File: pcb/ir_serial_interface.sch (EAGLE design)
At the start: 26 parts, among them IC1 PIC18F2550_28W, Q1 BSS123, T1 SFH303

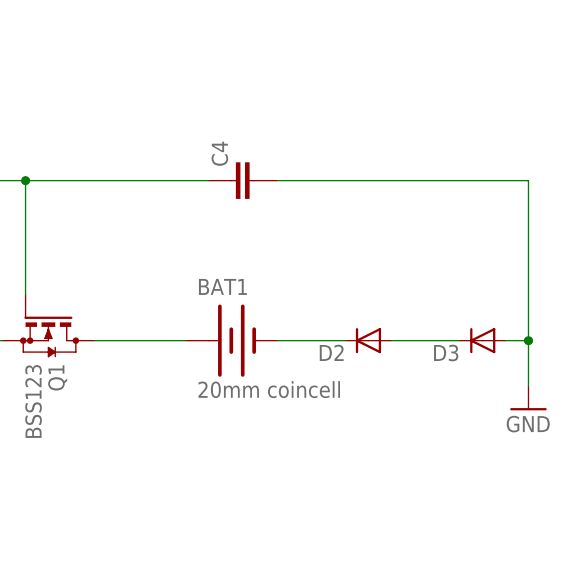
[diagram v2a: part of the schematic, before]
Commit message: sleep longer after fsk tx
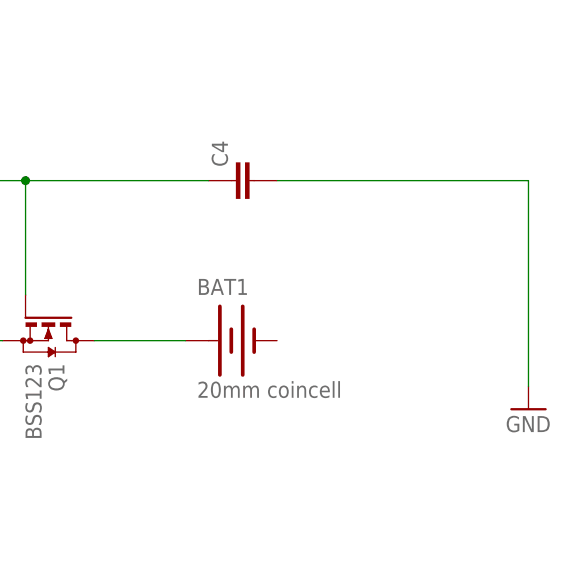
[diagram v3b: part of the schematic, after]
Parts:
- removed D2, D3: (no value), SparkFun-DiscreteSemi:DIODESOT23
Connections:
- removed net N$12: BAT1.-, D2.C
- removed net N$13: D2.A, D3.C
- net GND: no longer D3.A
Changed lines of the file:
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@@
 <part name="R8" library="resistor" deviceset="R-EU_" device="M0805" value="190"/>
 <part name="BAT1" library="SparkFun-Electromechanical" deviceset="BATTERY" device="20PTH" value="20mm coincell"/>
-<part name="D2" library="SparkFun-DiscreteSemi" deviceset="DIODE" device="SOT23"/>
-<part name="D3" library="SparkFun-DiscreteSemi" deviceset="DIODE" device="SOT23"/>
 <part name="P+5" library="supply1" deviceset="+5V" device=""/>
 <part name="GND10" library="supply1" deviceset="GND" device=""/>
@@
 <instance part="R8" gate="G$1" x="134.62" y="60.96" rot="R90"/>
 <instance part="BAT1" gate="G$1" x="289.56" y="12.7"/>
-<instance part="D2" gate="G$1" x="304.8" y="12.7" rot="R180"/>
-<instance part="D3" gate="G$1" x="317.5" y="12.7" rot="R180"/>
 <instance part="P+5" gate="1" x="251.46" y="22.86"/>
 <instance part="GND10" gate="1" x="322.58" y="5.08"/>
@@
 </segment>
 <segment>
-<pinref part="D3" gate="G$1" pin="A"/>
 <pinref part="GND10" gate="1" pin="GND"/>
-<wire x1="320.04" y1="12.7" x2="322.58" y2="12.7" width="0.1524" layer="91"/>
-<wire x1="322.58" y1="12.7" x2="322.58" y2="7.62" width="0.1524" layer="91"/>
 <pinref part="C4" gate="G$1" pin="2"/>
 <wire x1="294.64" y1="30.48" x2="322.58" y2="30.48" width="0.1524" layer="91"/>
-<wire x1="322.58" y1="30.48" x2="322.58" y2="12.7" width="0.1524" layer="91"/>
-<junction x="322.58" y="12.7"/>
+<wire x1="322.58" y1="30.48" x2="322.58" y2="7.62" width="0.1524" layer="91"/>
 </segment>
 <segment>
@@
 </segment>
 </net>
-<net name="N$12" class="0">
-<segment>
-<pinref part="BAT1" gate="G$1" pin="-"/>
-<pinref part="D2" gate="G$1" pin="C"/>
-<wire x1="294.64" y1="12.7" x2="302.26" y2="12.7" width="0.1524" layer="91"/>
-</segment>
-</net>
-<net name="N$13" class="0">
-<segment>
-<pinref part="D2" gate="G$1" pin="A"/>
-<pinref part="D3" gate="G$1" pin="C"/>
-<wire x1="307.34" y1="12.7" x2="314.96" y2="12.7" width="0.1524" layer="91"/>
-</segment>
-</net>

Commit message: multical iii docs + pcb
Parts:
- R4: value 200k -> 100k; device resistor:R-TRIMM3214W -> resistor:R-EU_M0805
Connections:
- net GND: now also R4.1; no longer R4.E
- net N$6: now also R4.2; no longer R4.S
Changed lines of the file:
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@@
 <part name="P+5" library="supply1" deviceset="+5V" device=""/>
 <part name="GND10" library="supply1" deviceset="GND" device=""/>
-<part name="R4" library="resistor" deviceset="R-TRIMM" device="3214W" value="200k"/>
 <part name="R9" library="resistor" deviceset="R-EU_" device="M0805" value="190"/>
 <part name="D4" library="led" deviceset="LED" device="3MM" value="IR"/>
@@
 <part name="Q1" library="transistor-small-signal" deviceset="BSS123" device=""/>
 <part name="C4" library="rcl" deviceset="C-EU" device="C0805"/>
+<part name="R4" library="resistor" deviceset="R-EU_" device="M0805" value="100k"/>
 </parts>
 <sheets>
@@
 <instance part="P+4" gate="1" x="203.2" y="96.52"/>
 <instance part="GND4" gate="1" x="226.06" y="53.34"/>
-<instance part="GND5" gate="1" x="198.12" y="53.34"/>
+<instance part="GND5" gate="1" x="203.2" y="53.34"/>
 <instance part="GND6" gate="1" x="185.42" y="53.34"/>
 <instance part="C3" gate="G$1" x="205.74" y="129.54" rot="R90"/>
@@
 <instance part="P+5" gate="1" x="251.46" y="22.86"/>
 <instance part="GND10" gate="1" x="322.58" y="5.08"/>
-<instance part="R4" gate="G$1" x="198.12" y="63.5"/>
 <instance part="R9" gate="G$1" x="137.16" y="48.26" rot="R90"/>
 <instance part="D4" gate="G$1" x="142.24" y="53.34" rot="R90"/>
@@
 <instance part="Q1" gate="G$1" x="269.24" y="12.7" rot="R270"/>
 <instance part="C4" gate="G$1" x="289.56" y="30.48" rot="R90"/>
+<instance part="R4" gate="G$1" x="203.2" y="66.04" rot="R90"/>
 </instances>
 <busses>
@@
 </segment>
 <segment>
-<pinref part="R4" gate="G$1" pin="E"/>
-<pinref part="GND5" gate="1" pin="GND"/>
-<wire x1="198.12" y1="58.42" x2="198.12" y2="55.88" width="0.1524" layer="91"/>
-</segment>
-<segment>
 <pinref part="D4" gate="G$1" pin="C"/>
 <pinref part="GND11" gate="1" pin="GND"/>
 <wire x1="147.32" y1="53.34" x2="149.86" y2="53.34" width="0.1524" layer="91"/>
 <wire x1="149.86" y1="53.34" x2="149.86" y2="50.8" width="0.1524" layer="91"/>
+</segment>
+<segment>
+<pinref part="R4" gate="G$1" pin="1"/>
+<pinref part="GND5" gate="1" pin="GND"/>
+<wire x1="203.2" y1="60.96" x2="203.2" y2="55.88" width="0.1524" layer="91"/>
 </segment>
 </net>
@@
 <pinref part="IC1" gate="G$1" pin="RA0/AN0"/>
 <wire x1="50.8" y1="35.56" x2="55.88" y2="35.56" width="0.1524" layer="91"/>
-<pinref part="R4" gate="G$1" pin="S"/>
-<wire x1="203.2" y1="63.5" x2="203.2" y2="73.66" width="0.1524" layer="91"/>
-</segment>
-</net>
+<pinref part="R4" gate="G$1" pin="2"/>
+<wire x1="203.2" y1="71.12" x2="203.2" y2="73.66" width="0.1524" layer="91"/>
+</segment>
+</net>

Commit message: PCB: board layout done
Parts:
- removed GND, LEFT, MIC, RIGHT: LSP10, solpad:LSP10
- removed Q1: BSS123, transistor-small-signal:BSS123
- added D2: (no value), semicon-smd-ipc:D-A1-C3
- added IC2: LP2992, texas:TPS77001
- added Q2: BC847SMD, transistor-npn:BC847SMD
- added R10: 2k, resistor:R-EU_M0805
- added R11, R12, R13: 100k, resistor:R-EU_M0805
- added U$2: AUDIO-JACK3, SparkFun-Connectors:AUDIO-JACK3
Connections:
- new net N$12: D2.A, U$2.RING1
- new net N$13: IC2.!EN, Q2.E, R11.1
- new net N$18: C4.1, D2.C, R10.2
- new net V+: BAT1.+, IC2.IN, Q2.C, R13.2
- net +5V: now also IC2.OUT; no longer Q1.S
- net GND: now also BAT1.-, IC2.GND, R11.2, R12.1, U$2.RING2; no longer GND.MP
- net N$16: now also IC1.RA5/AN4/!SS!/HLVDIN/C2OUT, R12.2, R13.1; no longer BAT1.+, Q1.D
- net N$17: now also Q2.B, R10.1; no longer C4.1, Q1.G, RIGHT.MP
- net N$5: now also U$2.TIP; no longer LEFT.MP
- net N$7: now also U$2.EARTH; no longer MIC.MP
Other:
- moved on the sheet: BAT1, C1, C2, C3, C4, R3, R4, R5, R6, R7

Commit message: silk screen cleanup
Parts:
- removed D4: IR, led:LED3MM
- added D3: (no value), semicon-smd-ipc:D-A1-C3
- D1: value RED -> IR; device SparkFun-LED:LED-REDLILYPAD -> led:LED3MM
- D2: value (none) -> RED; device semicon-smd-ipc:D-A1-C3 -> SparkFun-LED:LED-REDLILYPAD
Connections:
- net GND: now also D2.C; no longer D4.C
- net N$10: now also D2.A; no longer D1.A
- net N$12: now also D3.A; no longer D2.A
- net N$14: now also D1.A; no longer D4.A
- net N$18: now also D3.C; no longer D2.C
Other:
- moved on the sheet: D1
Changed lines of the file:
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@@
 <part name="GND7" library="supply1" deviceset="GND" device=""/>
 <part name="GND8" library="supply1" deviceset="GND" device=""/>
-<part name="D1" library="SparkFun-LED" deviceset="LED-RED" device="LILYPAD" value="RED"/>
+<part name="D2" library="SparkFun-LED" deviceset="LED-RED" device="LILYPAD" value="RED"/>
 <part name="GND9" library="supply1" deviceset="GND" device=""/>
 <part name="R8" library="resistor" deviceset="R-EU_" device="M0805" value="190"/>
@@
 <part name="GND10" library="supply1" deviceset="GND" device=""/>
 <part name="R9" library="resistor" deviceset="R-EU_" device="M0805" value="190"/>
-<part name="D4" library="led" deviceset="LED" device="3MM" value="IR"/>
+<part name="D1" library="led" deviceset="LED" device="3MM" value="IR"/>
 <part name="GND11" library="supply1" deviceset="GND" device=""/>
 <part name="C4" library="rcl" deviceset="C-EU" device="C0805"/>
@@
 <part name="GND12" library="supply1" deviceset="GND" device=""/>
 <part name="Q2" library="transistor-npn" deviceset="BC847*" device="SMD"/>
-<part name="D2" library="semicon-smd-ipc" deviceset="D-" device="A1-C3"/>
+<part name="D3" library="semicon-smd-ipc" deviceset="D-" device="A1-C3"/>
 <part name="GND4" library="supply1" deviceset="GND" device=""/>
 <part name="R10" library="resistor" deviceset="R-EU_" device="M0805" value="2k"/>
@@
 <instance part="GND7" gate="1" x="86.36" y="58.42"/>
 <instance part="GND8" gate="1" x="68.58" y="58.42"/>
-<instance part="D1" gate="G$1" x="142.24" y="66.04" rot="R90"/>
+<instance part="D2" gate="G$1" x="142.24" y="66.04" rot="R90"/>
 <instance part="GND9" gate="1" x="149.86" y="60.96"/>
 <instance part="R8" gate="G$1" x="134.62" y="60.96" rot="R90"/>
@@
 <instance part="GND10" gate="1" x="172.72" y="63.5"/>
 <instance part="R9" gate="G$1" x="137.16" y="48.26" rot="R90"/>
-<instance part="D4" gate="G$1" x="142.24" y="53.34" rot="R90"/>
+<instance part="D1" gate="G$1" x="142.24" y="53.34" rot="R90"/>
 <instance part="GND11" gate="1" x="149.86" y="48.26"/>
 <instance part="C4" gate="G$1" x="172.72" y="78.74"/>
@@
 <instance part="GND12" gate="1" x="106.68" y="116.84"/>
 <instance part="Q2" gate="G$1" x="203.2" y="91.44"/>
-<instance part="D2" gate="G$1" x="162.56" y="91.44"/>
+<instance part="D3" gate="G$1" x="162.56" y="91.44"/>
 <instance part="GND4" gate="1" x="205.74" y="63.5"/>
 <instance part="R10" gate="G$1" x="185.42" y="91.44" rot="R180"/>
@@
 </segment>
 <segment>
-<pinref part="D1" gate="G$1" pin="C"/>
+<pinref part="D2" gate="G$1" pin="C"/>
 <pinref part="GND9" gate="1" pin="GND"/>
 <wire x1="147.32" y1="66.04" x2="149.86" y2="66.04" width="0.1524" layer="91"/>
@@
 </segment>
 <segment>
-<pinref part="D4" gate="G$1" pin="C"/>
+<pinref part="D1" gate="G$1" pin="C"/>
 <pinref part="GND11" gate="1" pin="GND"/>
 <wire x1="147.32" y1="53.34" x2="149.86" y2="53.34" width="0.1524" layer="91"/>
@@
 <net name="N$10" class="0">
 <segment>
-<pinref part="D1" gate="G$1" pin="A"/>
+<pinref part="D2" gate="G$1" pin="A"/>
 <pinref part="R8" gate="G$1" pin="2"/>
 <wire x1="139.7" y1="66.04" x2="134.62" y2="66.04" width="0.1524" layer="91"/>
@@
 <net name="N$14" class="0">
 <segment>
-<pinref part="D4" gate="G$1" pin="A"/>
+<pinref part="D1" gate="G$1" pin="A"/>
 <pinref part="R9" gate="G$1" pin="2"/>
 <wire x1="139.7" y1="53.34" x2="137.16" y2="53.34" width="0.1524" layer="91"/>
@@
 <net name="N$12" class="0">
 <segment>
-<pinref part="D2" gate="G$1" pin="A"/>
+<pinref part="D3" gate="G$1" pin="A"/>
 <wire x1="160.02" y1="91.44" x2="116.84" y2="91.44" width="0.1524" layer="91"/>
 <wire x1="116.84" y1="91.44" x2="116.84" y2="111.76" width="0.1524" layer="91"/>
@@
 <net name="N$18" class="0">
 <segment>
-<pinref part="D2" gate="G$1" pin="C"/>
+<pinref part="D3" gate="G$1" pin="C"/>
 <pinref part="R10" gate="G$1" pin="2"/>
 <wire x1="165.1" y1="91.44" x2="172.72" y2="91.44" width="0.1524" layer="91"/>

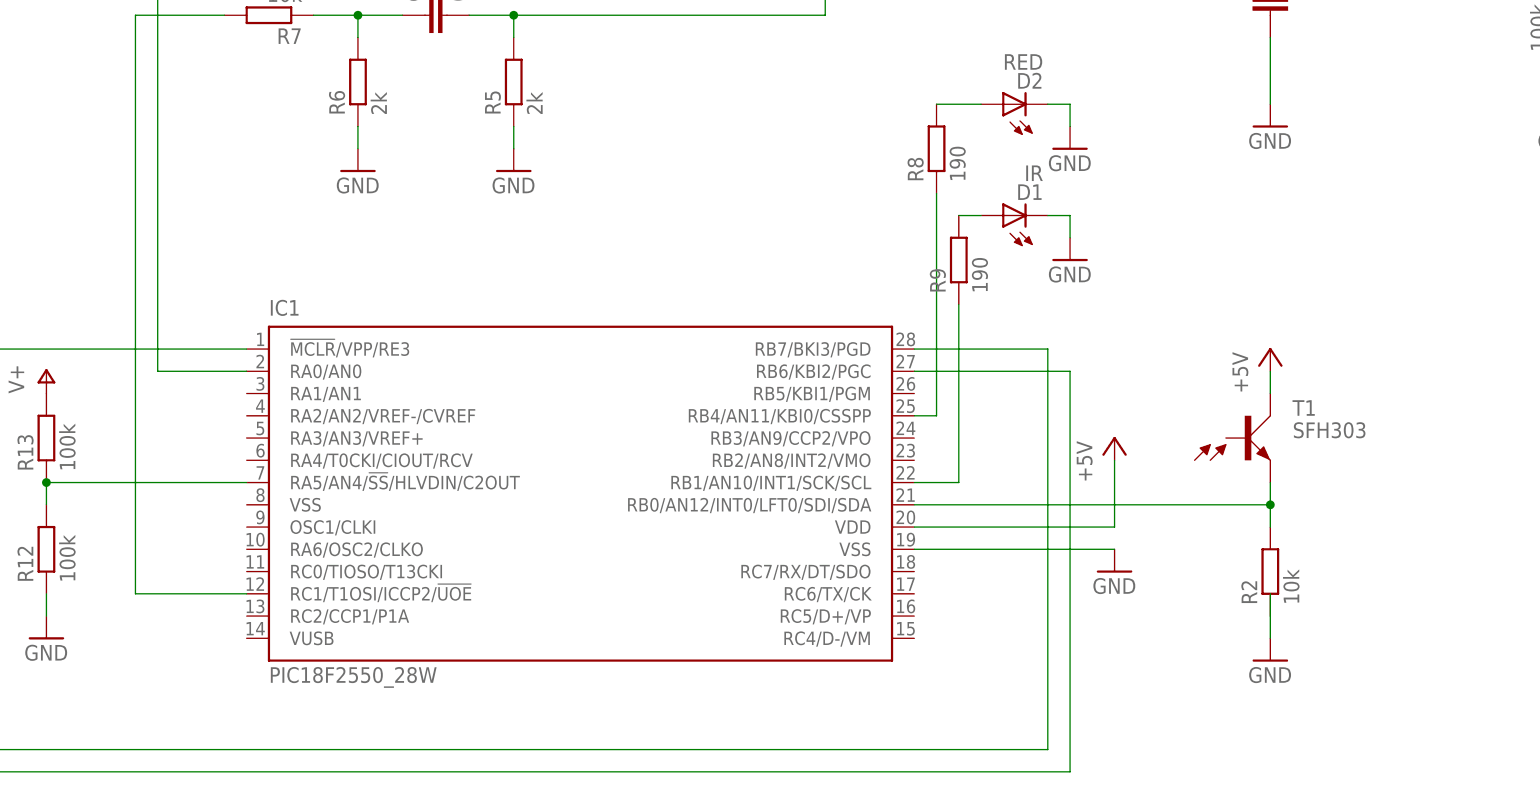
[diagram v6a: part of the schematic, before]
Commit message: cut round - wider outline path
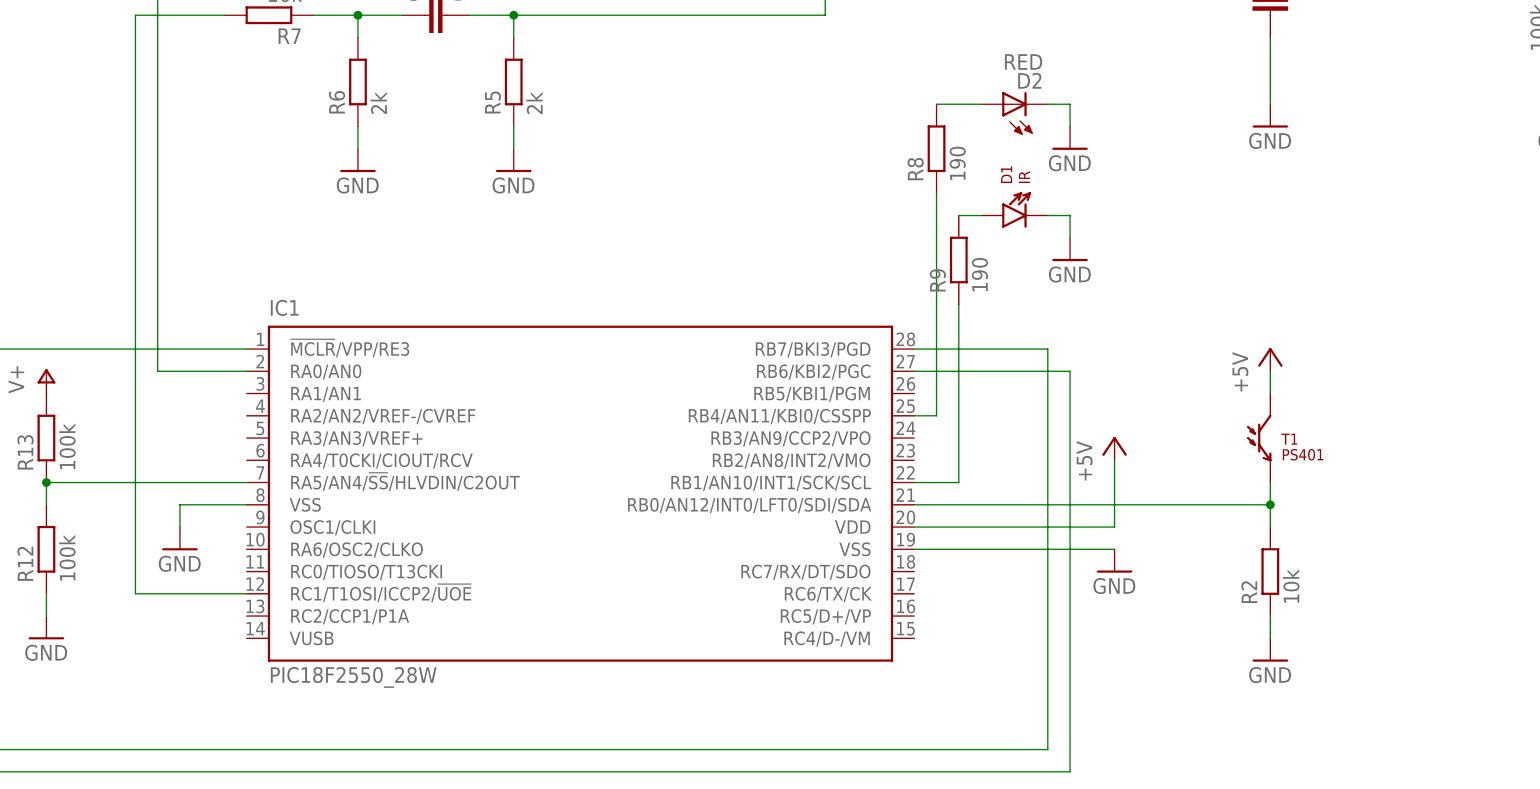
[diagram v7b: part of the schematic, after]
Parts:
- D1: device led:LED3MM -> SparkFun-LED:LTE-302
- T1: value SFH303 -> PS401; device opto-trans-siemens:SFH303 -> SparkFun-Sensors:LTR-301
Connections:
- net GND: now also IC1.VSS
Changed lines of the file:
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@@
 <layer number="54" name="bGND_GNDA" color="1" fill="9" visible="no" active="no"/>
 <layer number="56" name="wert" color="7" fill="1" visible="no" active="no"/>
+<layer number="57" name="tCAD" color="7" fill="1" visible="no" active="no"/>
 <layer number="91" name="Nets" color="2" fill="1" visible="yes" active="yes"/>
 <layer number="92" name="Busses" color="1" fill="1" visible="yes" active="yes"/>
@@
 <layer number="97" name="Info" color="7" fill="1" visible="yes" active="yes"/>
 <layer number="98" name="Guide" color="6" fill="1" visible="yes" active="yes"/>
+<layer number="99" name="SpiceOrder" color="7" fill="1" visible="yes" active="yes"/>
 <layer number="100" name="Muster" color="7" fill="1" visible="no" active="no"/>
 <layer number="101" name="Patch_Top" color="12" fill="4" visible="yes" active="yes"/>
@@
 <layer number="108" name="tplace-old" color="10" fill="1" visible="yes" active="yes"/>
 <layer number="109" name="ref-old" color="11" fill="1" visible="yes" active="yes"/>
+<layer number="110" name="fp0" color="7" fill="1" visible="yes" active="yes"/>
+<layer number="111" name="LPC17xx" color="7" fill="1" visible="yes" active="yes"/>
+<layer number="112" name="tSilk" color="7" fill="1" visible="yes" active="yes"/>
 <layer number="116" name="Patch_BOT" color="9" fill="4" visible="yes" active="yes"/>
 <layer number="121" name="_tsilk" color="7" fill="1" visible="yes" active="yes"/>
 <layer number="122" name="_bsilk" color="7" fill="1" visible="yes" active="yes"/>
+<layer number="123" name="tTestmark" color="7" fill="1" visible="yes" active="yes"/>
+<layer number="124" name="bTestmark" color="7" fill="1" visible="yes" active="yes"/>
 <layer number="125" name="_tNames" color="7" fill="1" visible="yes" active="yes"/>
+<layer number="126" name="_bNames" color="7" fill="1" visible="yes" active="yes"/>
+<layer number="127" name="_tValues" color="7" fill="1" visible="yes" active="yes"/>
+<layer number="128" name="_bValues" color="7" fill="1" visible="yes" active="yes"/>
+<layer number="131" name="tAdjust" color="7" fill="1" visible="yes" active="yes"/>
+<layer number="132" name="bAdjust" color="7" fill="1" visible="yes" active="yes"/>
 <layer number="144" name="Drill_legend" color="7" fill="1" visible="yes" active="yes"/>
+<layer number="150" name="Notes" color="7" fill="1" visible="yes" active="yes"/>
 <layer number="151" name="HeatSink" color="7" fill="1" visible="yes" active="yes"/>
+<layer number="152" name="_bDocu" color="7" fill="1" visible="yes" active="yes"/>
+<layer number="153" name="FabDoc1" color="7" fill="1" visible="yes" active="yes"/>
+<layer number="154" name="FabDoc2" color="7" fill="1" visible="yes" active="yes"/>
+<layer number="155" name="FabDoc3" color="7" fill="1" visible="yes" active="yes"/>
 <layer number="199" name="Contour" color="7" fill="1" visible="yes" active="yes"/>
 <layer number="200" name="200bmp" color="1" fill="10" visible="yes" active="yes"/>
@@
 <layer number="223" name="223bmp" color="24" fill="1" visible="no" active="no"/>
 <layer number="224" name="224bmp" color="25" fill="1" visible="no" active="no"/>
+<layer number="248" name="Housing" color="7" fill="1" visible="yes" active="yes"/>
+<layer number="249" name="Edge" color="7" fill="1" visible="yes" active="yes"/>
 <layer number="250" name="Descript" color="3" fill="1" visible="no" active="no"/>
 <layer number="251" name="SMDround" color="12" fill="11" visible="no" active="no"/>
@@
 </classes>
 <parts>
-<part name="T1" library="opto-trans-siemens" deviceset="SFH303" device=""/>
+<part name="T1" library="SparkFun-Sensors" deviceset="LTR-301" device="" value="PS401"/>
 <part name="P+1" library="supply1" deviceset="+5V" device=""/>
 <part name="GND1" library="supply1" deviceset="GND" device=""/>
@@
 <part name="GND10" library="supply1" deviceset="GND" device=""/>
 <part name="R9" library="resistor" deviceset="R-EU_" device="M0805" value="190"/>
-<part name="D1" library="led" deviceset="LED" device="3MM" value="IR"/>
+<part name="D1" library="SparkFun-LED" deviceset="LTE-302" device="" value="IR"/>
 <part name="GND11" library="supply1" deviceset="GND" device=""/>
 <part name="C4" library="rcl" deviceset="C-EU" device="C0805"/>
@@
 <part name="R12" library="resistor" deviceset="R-EU_" device="M0805" value="100k"/>
 <part name="R13" library="resistor" deviceset="R-EU_" device="M0805" value="100k"/>
+<part name="GND16" library="supply1" deviceset="GND" device=""/>
 </parts>
 <sheets>
@@
 </plain>
 <instances>
-<instance part="T1" gate="G$1" x="170.18" y="27.94"/>
+<instance part="T1" gate="G$1" x="172.72" y="30.48"/>
 <instance part="P+1" gate="1" x="154.94" y="27.94"/>
 <instance part="GND1" gate="1" x="154.94" y="12.7"/>
@@
 <instance part="R12" gate="G$1" x="33.02" y="15.24" rot="R90"/>
 <instance part="R13" gate="G$1" x="33.02" y="27.94" rot="R90"/>
+<instance part="GND16" gate="1" x="48.26" y="15.24"/>
 </instances>
 <busses>
@@
 <net name="GND" class="0">
 <segment>
-<pinref part="GND2" gate="1" pin="GND"/>
-<pinref part="R2" gate="G$1" pin="1"/>
-<wire x1="172.72" y1="5.08" x2="172.72" y2="7.62" width="0.1524" layer="91"/>
-<wire x1="172.72" y1="7.62" x2="172.72" y2="10.16" width="0.1524" layer="91"/>
-</segment>
-<segment>
 <pinref part="U$1" gate="G$1" pin="GND"/>
 <pinref part="GND3" gate="1" pin="GND"/>
@@
 <wire x1="33.02" y1="10.16" x2="33.02" y2="7.62" width="0.1524" layer="91"/>
 </segment>
+<segment>
+<pinref part="GND16" gate="1" pin="GND"/>
+<wire x1="48.26" y1="17.78" x2="48.26" y2="20.32" width="0.1524" layer="91"/>
+<pinref part="IC1" gate="G$1" pin="VSS"/>
+<wire x1="48.26" y1="20.32" x2="55.88" y2="20.32" width="0.1524" layer="91"/>
+</segment>
+<segment>
+<pinref part="R2" gate="G$1" pin="1"/>
+<pinref part="GND2" gate="1" pin="GND"/>
+<wire x1="172.72" y1="7.62" x2="172.72" y2="5.08" width="0.1524" layer="91"/>
+</segment>
 </net>
